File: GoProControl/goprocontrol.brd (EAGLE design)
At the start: 54.2 x 51.8 mm, 17 parts, among them Q1 IRLML6344

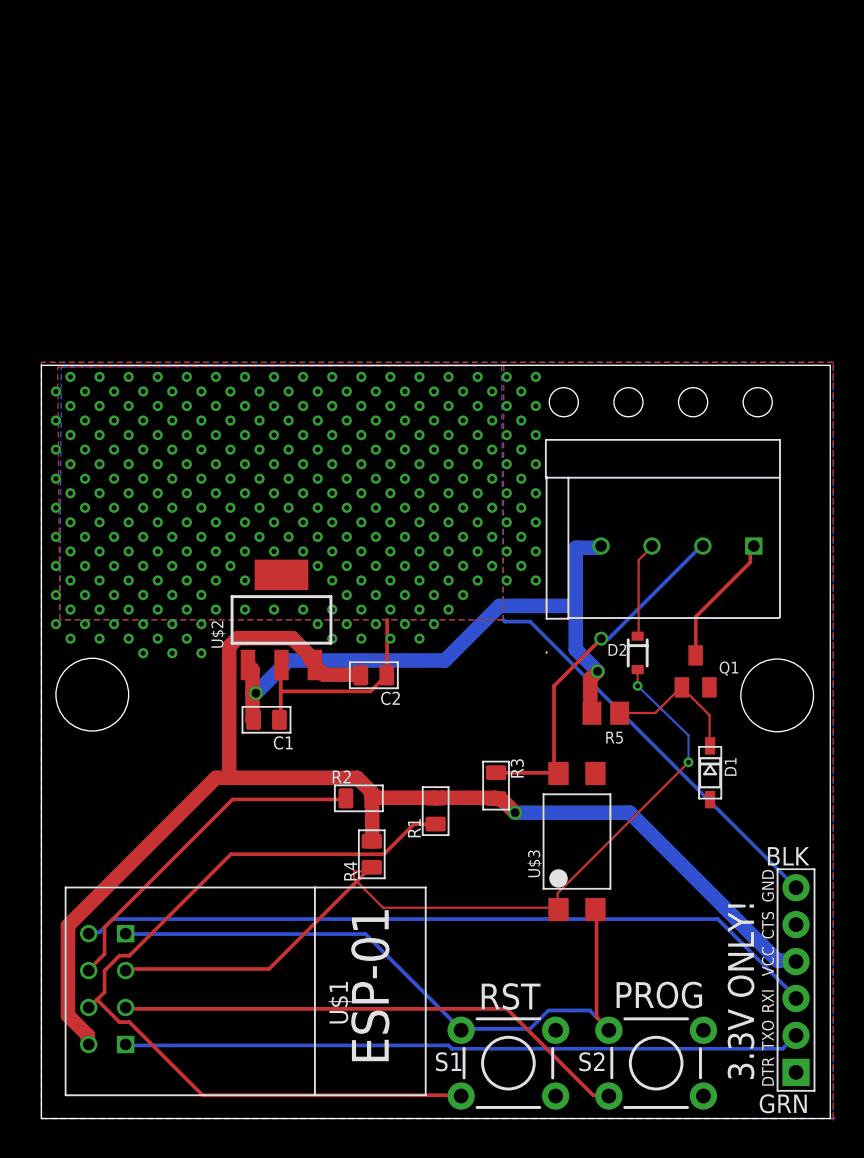
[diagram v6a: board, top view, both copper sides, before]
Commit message: Add a 500ma PTC fuse to protect things
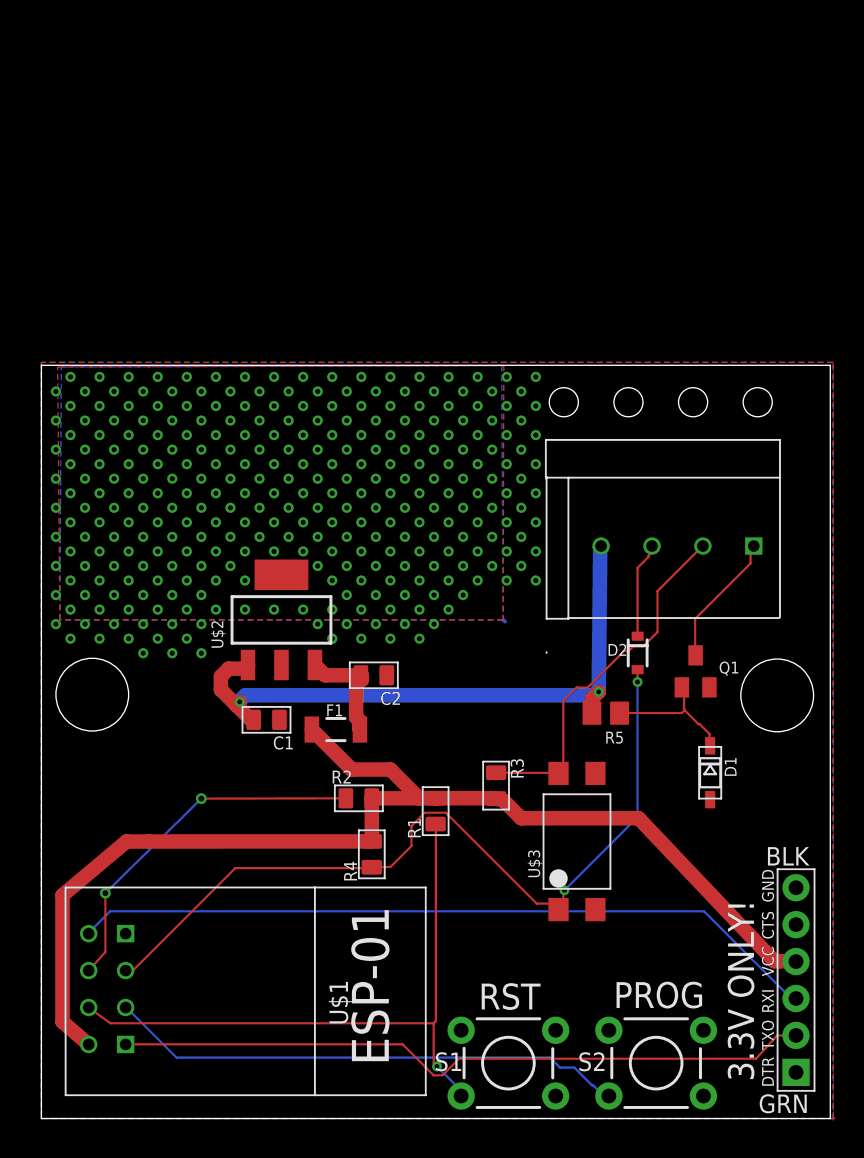
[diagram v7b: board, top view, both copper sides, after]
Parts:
- added F1: PTCSMD-W, SparkFun-PowerIC:PTC-1206-WIDE
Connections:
- new net 3.3-UNPRO: C2.2, F1.1, U$2.3
- net 3.3V: now also F1.2; no longer C2.2, U$2.3
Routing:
- net GND: track 89.0 -> 0.18 mm
- net N$3: track 57.7 -> 43.6 mm, vias 0 -> 1
- net 3.3V: track 91.0 -> 79.7 mm, vias 1 -> 0
- net 3.3-UNPRO: track 0.00 -> 7.50 mm
- net GPIO2: track 58.6 -> 56.6 mm
- net TXD: track 46.6 -> 48.1 mm
- net N$1: track 23.7 -> 25.0 mm, vias 0 -> 2
- net +12V: track 42.7 -> 43.3 mm
- net OUTPUT: track 24.8 -> 25.1 mm, vias 1 -> 0

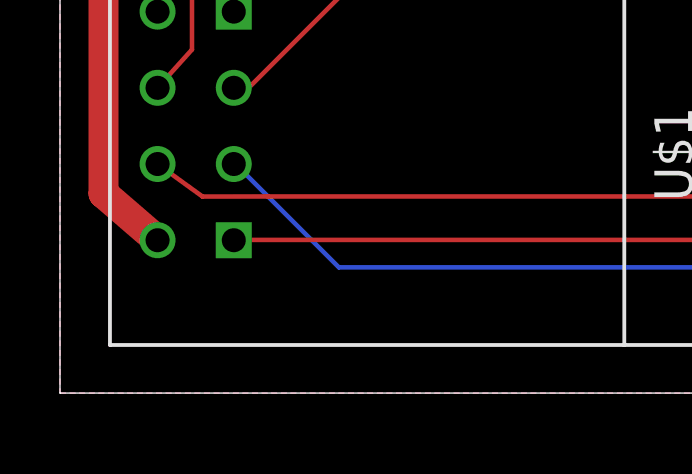
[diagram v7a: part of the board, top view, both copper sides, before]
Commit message: Add pullup on GPIO0 for better reliability and switch to 10K pullups
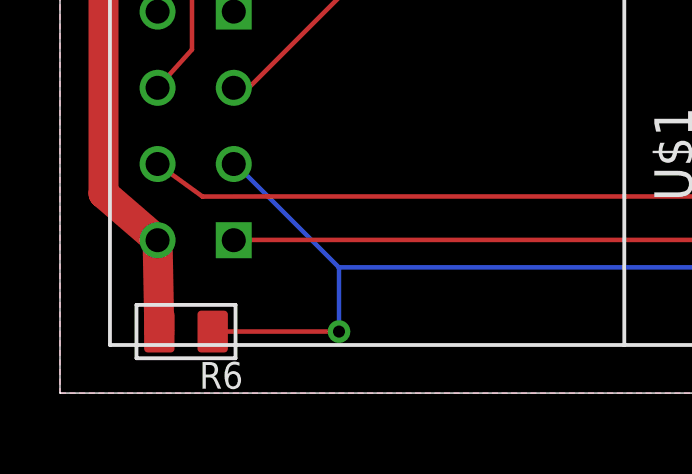
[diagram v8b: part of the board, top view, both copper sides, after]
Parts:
- added R6: 10K, Seeed-OPL-Resistor:R0805
- R1, R2, R3: value 1K -> 10K
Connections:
- net 3.3V: now also R6.2
- net GPIO0: now also R6.1
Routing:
- net GPIO0: track 35.8 -> 42.1 mm, vias 0 -> 1
- net 3.3V: track 79.7 -> 82.7 mm
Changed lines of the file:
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@@
 <attribute name="NAME" x="46.585" y="30.605" size="0.8128" layer="25"/>
 </element>
-<element name="R1" library="Seeed-OPL-Resistor" package="R0805" value="1K" x="27.11" y="21.14" smashed="yes" rot="R180">
-<attribute name="MPN" value="RC0805JR-071KL" x="27.11" y="21.14" size="1.778" layer="27" rot="R180" display="off"/>
+<element name="R1" library="Seeed-OPL-Resistor" package="R0805" value="10K" x="27.11" y="21.14" smashed="yes" rot="R180">
+<attribute name="MPN" value="RC0805FR-0710KL" x="27.11" y="21.14" size="1.778" layer="27" rot="R180" display="off"/>
 <attribute name="NAME" x="26.094" y="19.235" size="0.889" layer="25" font="vector" ratio="11" rot="R90"/>
 </element>
@@
 <attribute name="NAME" x="40.08" y="26.605" size="0.8128" layer="25" rot="R180"/>
 </element>
-<element name="R2" library="Seeed-OPL-Resistor" package="R0805" value="1K" x="21.83" y="22.02" smashed="yes" rot="R90">
-<attribute name="MPN" value="RC0805JR-071KL" x="21.83" y="22.02" size="1.778" layer="27" rot="R90" display="off"/>
+<element name="R2" library="Seeed-OPL-Resistor" package="R0805" value="10K" x="21.83" y="22.02" smashed="yes" rot="R90">
+<attribute name="MPN" value="RC0805FR-0710KL" x="21.83" y="22.02" size="1.778" layer="27" rot="R90" display="off"/>
 <attribute name="NAME" x="19.925" y="23.036" size="0.889" layer="25" font="vector" ratio="11"/>
 </element>
@@
 <attribute name="NAME" x="12.51" y="32.29" size="0.8128" layer="25" rot="R90"/>
 </element>
-<element name="R3" library="Seeed-OPL-Resistor" package="R0805" value="1K" x="31.265" y="22.895" smashed="yes">
-<attribute name="MPN" value="RC0805JR-071KL" x="31.265" y="22.895" size="1.778" layer="27" display="off"/>
+<element name="R3" library="Seeed-OPL-Resistor" package="R0805" value="10K" x="31.265" y="22.895" smashed="yes">
+<attribute name="MPN" value="RC0805FR-0710KL" x="31.265" y="22.895" size="1.778" layer="27" display="off"/>
 <attribute name="NAME" x="32.281" y="24.8" size="0.889" layer="25" font="vector" ratio="11" rot="R270"/>
 </element>
@@
 <element name="F1" library="SparkFun-PowerIC" package="PTC-1206-WIDE" value="PTCSMD-W" x="20.25" y="26.75" smashed="yes" rot="R180">
 <attribute name="NAME" x="20.774" y="28.48" size="0.8128" layer="25" rot="R180"/>
+</element>
+<element name="R6" library="Seeed-OPL-Resistor" package="R0805" value="10K" x="4.2" y="2.05" smashed="yes" rot="R270">
+<attribute name="MPN" value="RC0805FR-0710KL" x="4.2" y="2.05" size="1.778" layer="27" rot="R270" display="off"/>
+<attribute name="NAME" x="6.105" y="1.034" size="0.889" layer="25" font="vector" ratio="11" rot="R180"/>
 </element>
 </elements>
@@
 <wire x1="1.45" y1="15.35" x2="1.45" y2="6.65" width="1" layer="1"/>
 <wire x1="1.45" y1="6.65" x2="3.2525" y2="5.095" width="1" layer="1"/>
+<contactref element="R6" pad="2"/>
+<wire x1="3.311" y1="2.05" x2="3.2525" y2="5.095" width="1" layer="1"/>
 <wire x1="51.6326" y1="10.8204" x2="51.895" y2="10.795" width="0" layer="19" extent="1-1"/>
 </signal>
@@
 <wire x1="5.8674" y1="7.62" x2="5.7925" y2="7.635" width="0.1524" layer="16"/>
 <wire x1="39.0144" y1="1.6002" x2="39.0238" y2="1.5494" width="0.1524" layer="16"/>
+<contactref element="R6" pad="1"/>
+<wire x1="5.089" y1="2.05" x2="9.3" y2="2.05" width="0.1524" layer="1"/>
+<via x="9.3" y="2.05" extent="1-16" drill="0.4"/>
+<wire x1="9.3" y1="2.05" x2="9.2964" y2="4.191" width="0.1524" layer="16"/>
 </signal>
 <signal name="TXD">
